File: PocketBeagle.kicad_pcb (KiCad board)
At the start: 4 copper layers, 55 x 35 mm, 50 parts, among them SW1 POWER, U1 OSD3358-512M-BSM, U2 SN74LVC1G07DCK, U3 TPD4S012DRY, X1 10118192-0001LF, X2 MICROSD, Y1 24 MHz

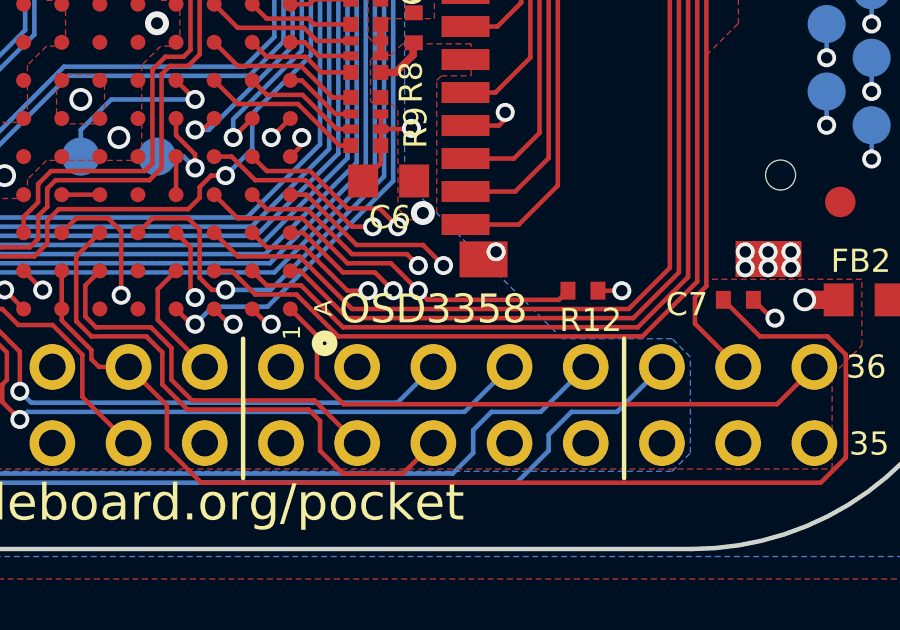
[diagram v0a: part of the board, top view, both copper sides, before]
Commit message: Pretty up the schematic and OSD component a bit
Signed-off-by: Michael Welling <mwelling@ieee.org>
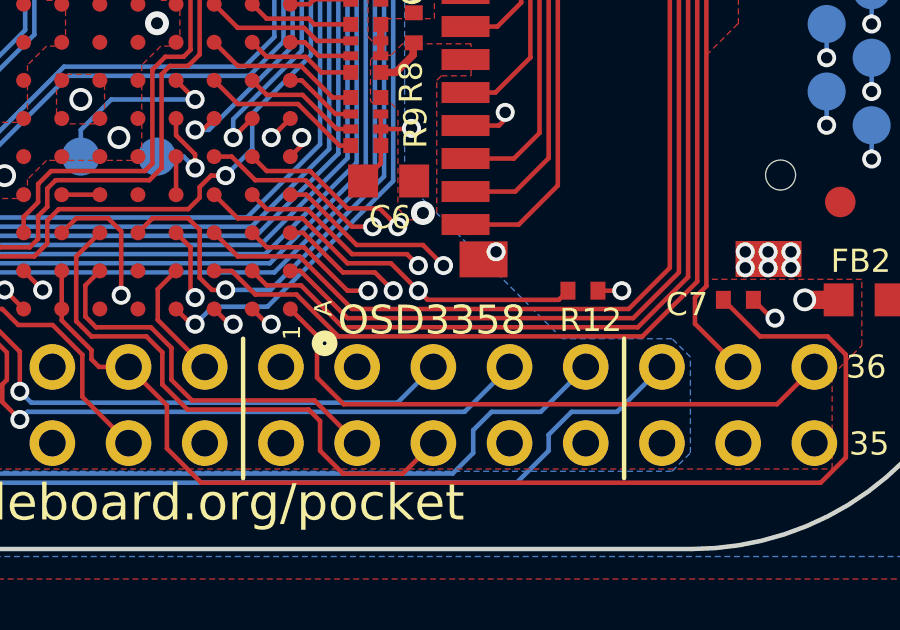
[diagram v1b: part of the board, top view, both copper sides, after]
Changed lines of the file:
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@@
   )
   (page A4)
+  (title_block
+    (title "PocketBeagle KiCAD")
+    (date 2017-08-14)
+    (comment 1 "Prototyped by: GHI Electronics, LLC")
+    (comment 2 "Converted to KiCAD: QWERTY Embedded Design, LLC")
+  )
   (layers
     (0 Top signal)
@@
   (gr_line (start 146.87042 108.23194) (end 146.40306 108.6993) (layer B.SilkS) (width 0.2))
   (gr_line (start 148.70176 108.23194) (end 146.87042 108.23194) (layer B.SilkS) (width 0.2))
-  (gr_text OSD3358 (at 154.2542 114.5032) (layer F.SilkS)
+  (gr_text OSD3358 (at 154.20594 114.87404) (layer F.SilkS)
     (effects (font (size 0.9652 0.9652) (thickness 0.1524)) (justify left))
   )
